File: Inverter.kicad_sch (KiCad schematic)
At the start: 50 parts, among them IC1 STGIPQ3H60T-HL, IC2 ACS724LLCTR-05AU-T

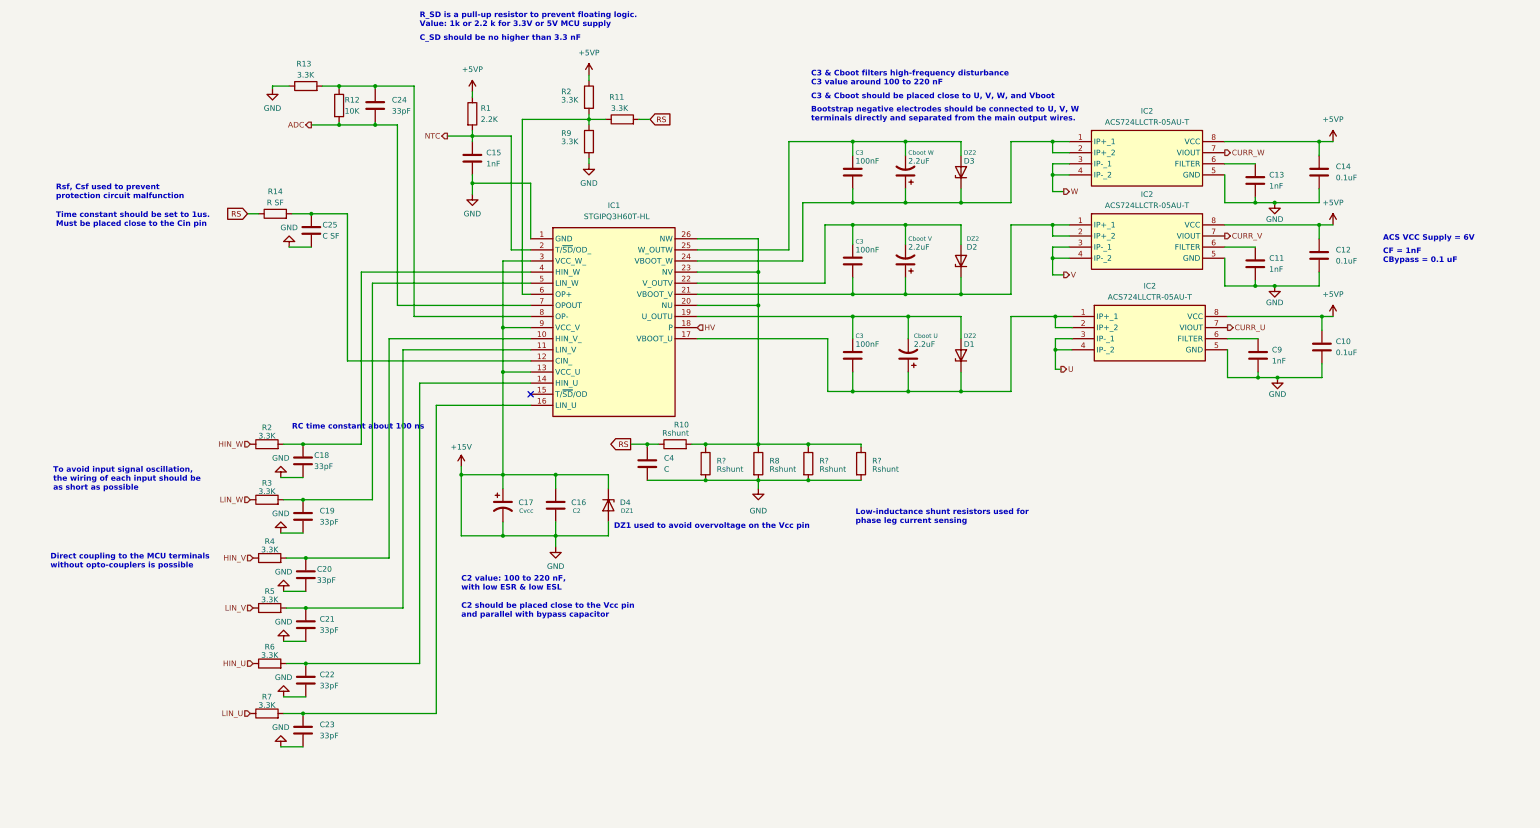
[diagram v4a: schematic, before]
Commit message: adding high speed isolator
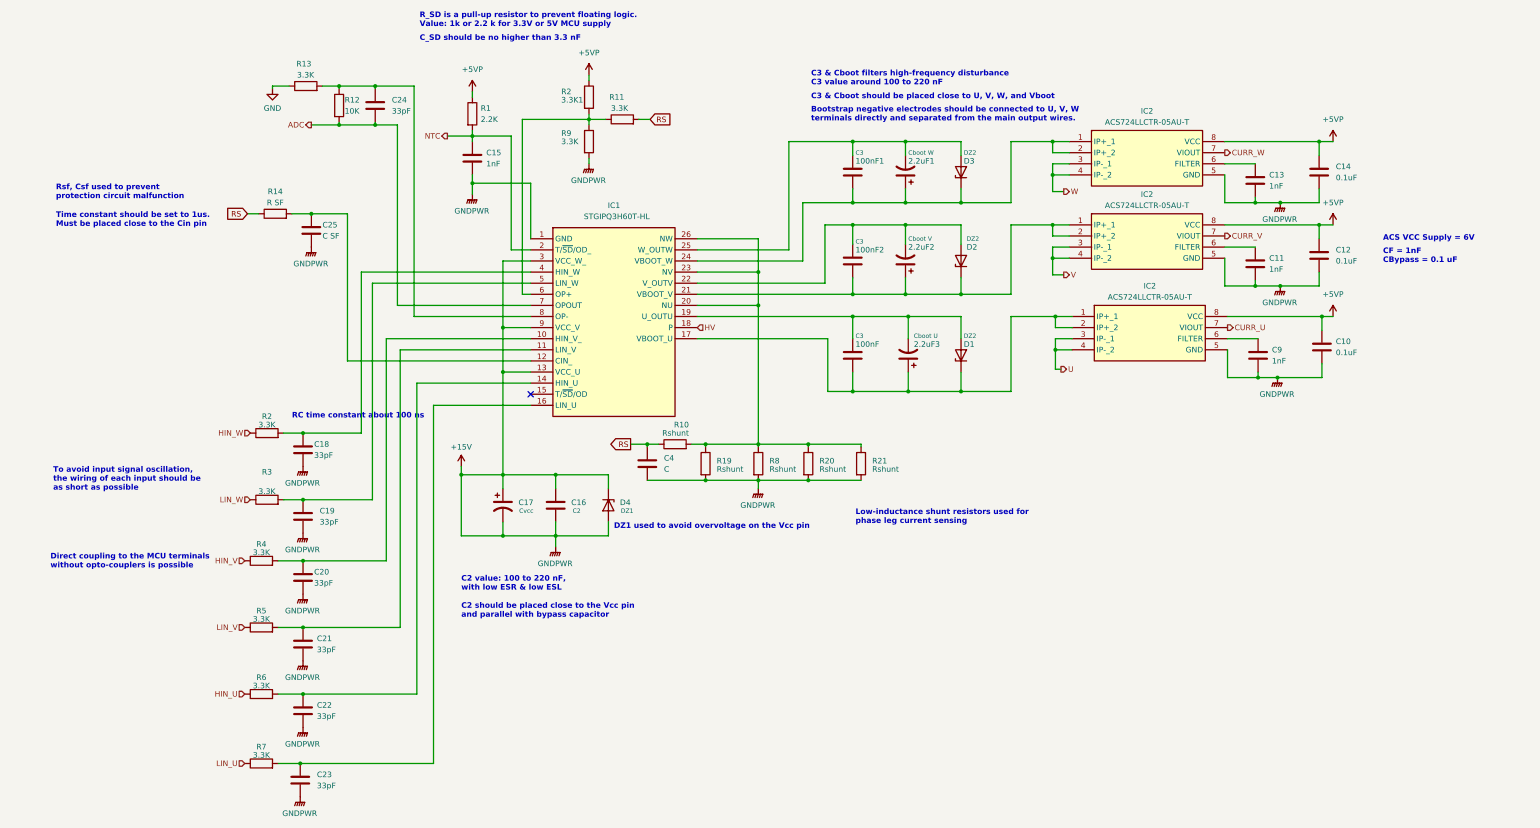
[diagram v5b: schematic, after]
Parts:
- IC1: footprint STGIPQ3H60THL -> SamacSys_Parts:STGIPQ3H60THL
- IC2: footprint SOIC127P600X175-8N -> SamacSys_Parts:SOIC127P600X175-8N
- gave numbers to parts that had none: 3
- renumbered 100nF to 100nF1, 100nF to 100nF2, 2.2uF to 2.2uF1, 2.2uF to 2.2uF2, 2.2uF to 2.2uF3, 3.3K to 3.3K1
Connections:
- net +15V: no longer R13.1
- new net GND: R13.1
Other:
- moved on the sheet: C18, C20, C21, C22, C23, R2, R4, R5, R6, R7

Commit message: updating component & board
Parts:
- removed 100nF1, 100nF2: C3, symbol Device:C
- removed 3.3K1: R2, symbol Device:R
- added C37, C38: 100n, symbol Device:C
- added C39: 0.1u, symbol Device:C
- added D4: LED, symbol Device:LED
- added R22: 3.3K, symbol Device:R
- added R23: 5k6, symbol Device:R
- added R24: 4k7, symbol Device:R
- C16: value C2 -> 100n
- C17: value Cvcc -> 10u 50V
- C18, C19, C20, C21, C22, C23: value 33pF -> 10pF
- C25: value C SF -> 1nF
- C3: value 100nF -> 100n
- CbootU1: renamed from 2.2uF3; value Cboot U -> 2.2u
- CbootV1: renamed from 2.2uF2; value Cboot V -> 2.2u
- CbootW1: renamed from 2.2uF1; value Cboot W -> 2.2u
- D1, D2, D3: value DZ2 -> MMSZ5250B
- DZ1: renamed from D4; value DZ1 -> MMSZ5250B
- R14: value R SF -> 1K
- R2, R3, R4, R5, R6, R7: value 3.3K -> 1K
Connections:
- net +15V: now also R11.2, C39.2, D4.2 (A), R23.2, R24.1; no longer R9.2
- net +5VP: now also R22.1
- net HV: now also C39.1
- net RS: now also R9.1; no longer R11.2
- net at CbootU1.1, IC1.17 (VBOOT_U), IC2.1 (IP+_1)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: now also D2.1 (K), C38.2; no longer C3.2, D1.1 (K)
- net at CbootU1.2, IC1.19 (U_OUTU): now also D2.2 (A), C38.1; no longer C3.1, D1.2 (A)
- net at IC1.6 (OP+), R11.1: now also R9.2, R22.2; no longer R9.1
- net at CbootW1.1, D3.1 (K), IC1.24 (VBOOT_W)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: now also C37.2
- net at CbootW1.2, D3.2 (A), IC1.25 (W_OUTW): now also C37.1
- net at CbootV1.1, IC1.21 (VBOOT_V), IC2.1 (IP+_1)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: now also C3.2, D1.1 (K); no longer D2.1 (K)
- net at CbootV1.2, IC1.22 (V_OUTV): now also C3.1, D1.2 (A); no longer D2.2 (A)
- net at C25.1, IC1.12 (CIN_), R14.2: now also R24.2
- new net: D4.1 (K), R23.1
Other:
- note added: "R24 value depend on shunt resistor"
- moved on the sheet: C16, C17, C25, DZ1, R14

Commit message: update footprint
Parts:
- removed R21: Rshunt, symbol Device:R
- D4: footprint (none) -> LED_THT:LED_D5.0mm
- IC2: footprint SamacSys_Parts:SOIC127P600X175-8N -> (none)
- R1, R11, R12, R13, R14, R2, R22, R23, R24, R3, R4, R5, R6, R7, R9: footprint (none) -> Resistor_THT:R_Axial_DIN0309_L9.0mm_D3.2mm_P12.70mm_Horizontal
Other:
- note added: "Shunt calculation: 1.5A * RS = 0.54 RS = 0.36"
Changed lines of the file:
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@@
   (junction (at 121.92 112.395) (diameter 0) (color 0 0 0 0)
   )
-  (junction (at 158.75 112.395) (diameter 0) (color 0 0 0 0)
-  )
   (junction (at 51.435 30.48) (diameter 0) (color 0 0 0 0)
   )
@@
   )
   (junction (at 34.925 59.69) (diameter 0) (color 0 0 0 0)
-  )
-  (junction (at 158.75 120.65) (diameter 0) (color 0 0 0 0)
   )
   (junction (at 43.18 125.095) (diameter 0) (color 0 0 0 0)
@@
     (stroke (width 0) (type default))
   )
-  (wire (pts (xy 158.75 120.65) (xy 170.815 120.65))
-    (stroke (width 0) (type default))
-  )
   (wire (pts (xy 37.465 154.305) (xy 43.18 154.305))
     (stroke (width 0) (type default))
@@
     (stroke (width 0) (type default))
   )
-  (wire (pts (xy 170.815 112.395) (xy 170.815 113.03))
-    (stroke (width 0) (type default))
-  )
   (wire (pts (xy 121.92 112.395) (xy 121.92 113.03))
     (stroke (width 0) (type default))
@@
   )
   (wire (pts (xy 276.225 93.98) (xy 276.225 97.155))
-    (stroke (width 0) (type default))
-  )
-  (wire (pts (xy 158.75 112.395) (xy 170.815 112.395))
     (stroke (width 0) (type default))
   )
@@
     (effects (font (size 1.27 1.27) bold) (justify left bottom))
   )
+  (text "Shunt calculation:\n1.5A * RS = 0.54\nRS = 0.36" (at 163.83 125.73 0)
+    (effects (font (size 1.27 1.27) bold) (justify left bottom))
+  )
   (text "To avoid input signal oscillation, \nthe wiring of each input should be \nas short as possible\n"
     (at -13.97 123.19 0)
@@
   )
   (text "Low-inductance shunt resistors used for \nphase leg current sensing"
-    (at 169.545 130.81 0)
+    (at 154.305 109.855 0)
     (effects (font (size 1.27 1.27) bold) (justify left bottom))
   )
@@
       (effects (font (size 1.27 1.27)) (justify right))
     )
-    (property "Footprint" "" (at 85.09 125.095 0)
+    (property "Footprint" "LED_THT:LED_D5.0mm" (at 85.09 125.095 0)
       (effects (font (size 1.27 1.27)) hide)
     )
@@
       (effects (font (size 1.27 1.27)))
     )
-    (property "Footprint" "" (at 33.655 140.843 90)
+    (property "Footprint" "Resistor_THT:R_Axial_DIN0309_L9.0mm_D3.2mm_P12.70mm_Horizontal" (at 33.655 140.843 90)
       (effects (font (size 1.27 1.27)) hide)
     )
@@
       (effects (font (size 1.27 1.27)))
     )
-    (property "Footprint" "" (at 34.925 111.633 90)
+    (property "Footprint" "Resistor_THT:R_Axial_DIN0309_L9.0mm_D3.2mm_P12.70mm_Horizontal" (at 34.925 111.633 90)
       (effects (font (size 1.27 1.27)) hide)
     )
@@
       (effects (font (size 1.27 1.27)) (justify left))
     )
-    (property "Footprint" "" (at 49.657 34.925 90)
+    (property "Footprint" "Resistor_THT:R_Axial_DIN0309_L9.0mm_D3.2mm_P12.70mm_Horizontal" (at 49.657 34.925 90)
       (effects (font (size 1.27 1.27)) hide)
     )
@@
     )
     (property "Value" "Rshunt" (at 161.29 118.11 0)
-      (effects (font (size 1.27 1.27)) (justify left))
+      (effects (font (size 1.27 1.27)) (justify left) hide)
     )
     (property "Footprint" "" (at 156.972 116.84 90)
@@
       (effects (font (size 1.27 1.27)))
     )
-    (property "Footprint" "" (at 33.655 156.083 90)
+    (property "Footprint" "Resistor_THT:R_Axial_DIN0309_L9.0mm_D3.2mm_P12.70mm_Horizontal" (at 33.655 156.083 90)
       (effects (font (size 1.27 1.27)) hide)
     )
@@
       (effects (font (size 1.27 1.27)) (justify left))
     )
-    (property "Footprint" "" (at 83.312 134.62 90)
+    (property "Footprint" "Resistor_THT:R_Axial_DIN0309_L9.0mm_D3.2mm_P12.70mm_Horizontal" (at 83.312 134.62 90)
       (effects (font (size 1.27 1.27)) hide)
     )
@@
       (effects (font (size 1.27 1.27)))
     )
-    (property "Footprint" "" (at 33.655 171.323 90)
+    (property "Footprint" "Resistor_THT:R_Axial_DIN0309_L9.0mm_D3.2mm_P12.70mm_Horizontal" (at 33.655 171.323 90)
       (effects (font (size 1.27 1.27)) hide)
     )
@@
       (effects (font (size 1.27 1.27)) (justify left))
     )
-    (property "Footprint" "" (at 106.807 43.18 90)
+    (property "Footprint" "Resistor_THT:R_Axial_DIN0309_L9.0mm_D3.2mm_P12.70mm_Horizontal" (at 106.807 43.18 90)
       (effects (font (size 1.27 1.27)) hide)
     )
@@
       (effects (font (size 1.27 1.27)))
     )
-    (property "Footprint" "" (at 33.655 187.198 90)
+    (property "Footprint" "Resistor_THT:R_Axial_DIN0309_L9.0mm_D3.2mm_P12.70mm_Horizontal" (at 33.655 187.198 90)
       (effects (font (size 1.27 1.27)) hide)
     )
@@
       (effects (font (size 1.27 1.27)))
     )
-    (property "Footprint" "" (at 34.925 126.873 90)
+    (property "Footprint" "Resistor_THT:R_Axial_DIN0309_L9.0mm_D3.2mm_P12.70mm_Horizontal" (at 34.925 126.873 90)
       (effects (font (size 1.27 1.27)) hide)
     )
@@
       (effects (font (size 1.27 1.27)) (justify left))
     )
-    (property "Footprint" "" (at 80.137 36.83 90)
+    (property "Footprint" "Resistor_THT:R_Axial_DIN0309_L9.0mm_D3.2mm_P12.70mm_Horizontal" (at 80.137 36.83 90)
       (effects (font (size 1.27 1.27)) hide)
     )
@@
       (effects (font (size 1.27 1.27)))
     )
-    (property "Footprint" "SamacSys_Parts:SOIC127P600X175-8N" (at 250.19 138.1 0)
+    (property "Footprint" "" (at 250.19 138.1 0)
       (effects (font (size 1.27 1.27)) (justify left top) hide)
     )
@@
       (effects (font (size 1.27 1.27)) (justify left))
     )
-    (property "Footprint" "" (at 116.205 36.322 90)
+    (property "Footprint" "Resistor_THT:R_Axial_DIN0309_L9.0mm_D3.2mm_P12.70mm_Horizontal" (at 116.205 36.322 90)
       (effects (font (size 1.27 1.27)) hide)
     )
@@
       (effects (font (size 1.27 1.27)) (justify left))
     )
-    (property "Footprint" "" (at 43.815 32.258 90)
+    (property "Footprint" "Resistor_THT:R_Axial_DIN0309_L9.0mm_D3.2mm_P12.70mm_Horizontal" (at 43.815 32.258 90)
       (effects (font (size 1.27 1.27)) hide)
     )
@@
     )
   )
-  (symbol (lib_id "Device:R") (at 170.815 116.84 0) (unit 1)
-    (in_bom yes) (on_board yes) (dnp no)
-    (property "Reference" "R21" (at 173.355 116.205 0)
-      (effects (font (size 1.27 1.27)) (justify left))
-    )
-    (property "Value" "Rshunt" (at 173.355 118.11 0)
-      (effects (font (size 1.27 1.27)) (justify left))
-    )
-    (property "Footprint" "" (at 169.037 116.84 90)
-      (effects (font (size 1.27 1.27)) hide)
-    )
-    (property "Datasheet" "~" (at 170.815 116.84 0)
-      (effects (font (size 1.27 1.27)) hide)
-    )
-    (pin "1")
-    (pin "2")
-    (instances
-      (project "Main"
-        (path "/c97a22ab-71f8-4b91-b313-15b8a3e640d7/fb44c483-375e-43d2-9d1e-806996239436"
-          (reference "R21") (unit 1)
-        )
-      )
-    )
-  )
   (symbol (lib_id "Device:R") (at 108.585 33.02 0) (unit 1)
     (in_bom yes) (on_board yes) (dnp no)
@@
       (effects (font (size 1.27 1.27)) (justify left))
     )
-    (property "Footprint" "" (at 106.807 33.02 90)
+    (property "Footprint" "Resistor_THT:R_Axial_DIN0309_L9.0mm_D3.2mm_P12.70mm_Horizontal" (at 106.807 33.02 90)
       (effects (font (size 1.27 1.27)) hide)
     )
@@
       (effects (font (size 1.27 1.27)))
     )
-    (property "Footprint" "" (at 25.4 61.468 90)
+    (property "Footprint" "Resistor_THT:R_Axial_DIN0309_L9.0mm_D3.2mm_P12.70mm_Horizontal" (at 25.4 61.468 90)
       (effects (font (size 1.27 1.27)) hide)
     )
@@
       (effects (font (size 1.27 1.27)))
     )
-    (property "Footprint" "" (at 36.703 64.77 90)
-      (effects (font (size 1.27 1.27)) hide)
-    )
+    (property "Footprint" "Resistor_THT:R_Axial_DIN0309_L9.0mm_D3.2mm_P12.70mm_Horizontal" (at 36.703 64.77 90)
+      (effects (font (size 1.27 1.27)) hide)
+    )
